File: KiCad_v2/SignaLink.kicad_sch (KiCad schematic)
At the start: 15 parts, among them SW1 SW_Wake, U2 ESP32-C3_SUPERMINI_TH, U3 DM-OLED096-636

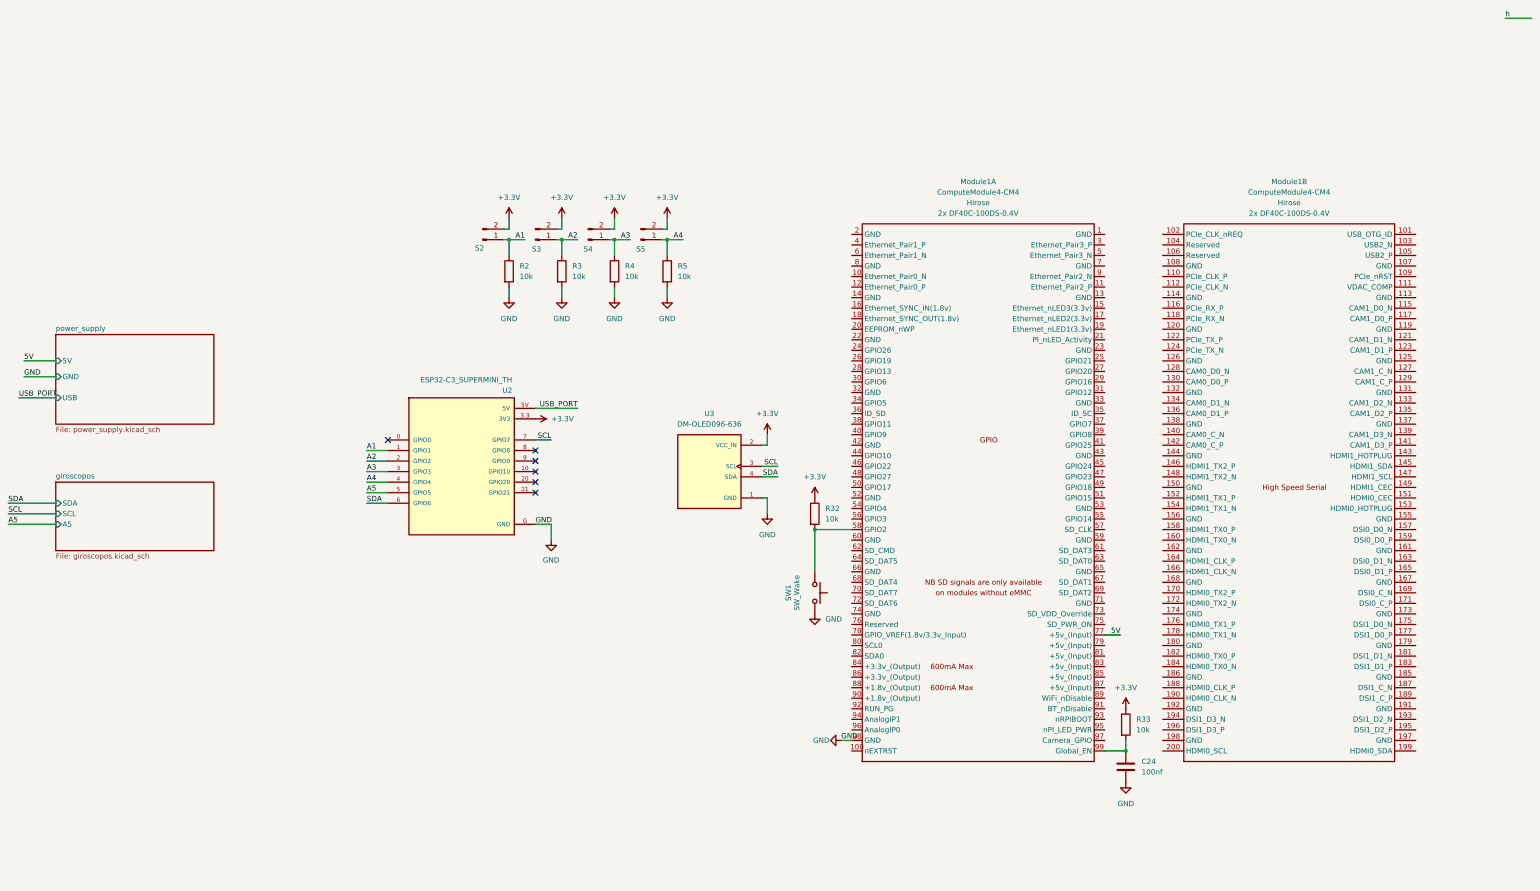
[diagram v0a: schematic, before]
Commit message: feat: huella cm4 y mcp symbols
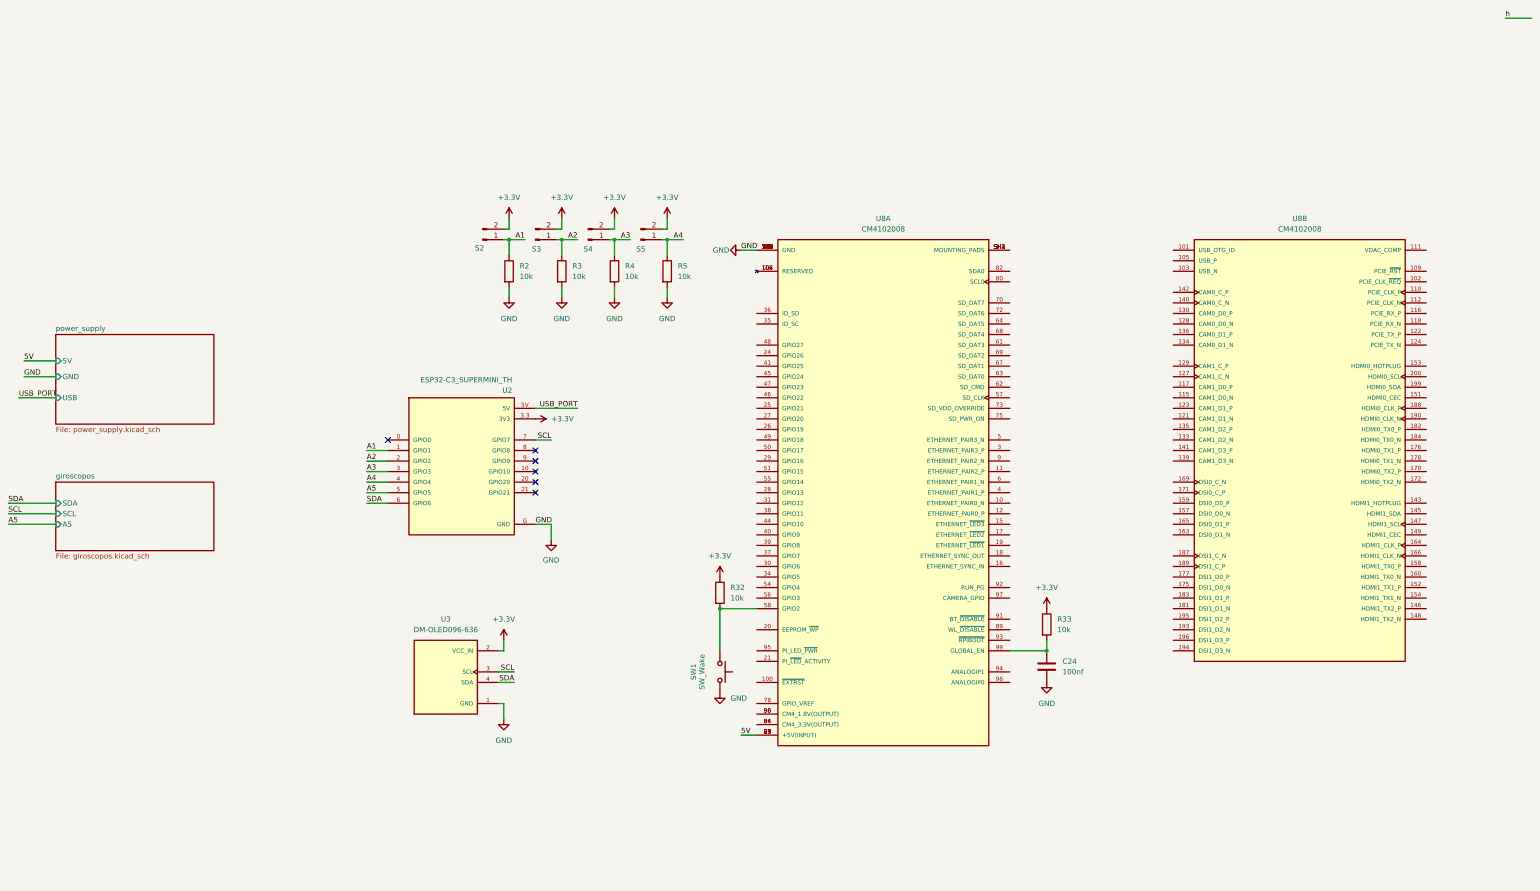
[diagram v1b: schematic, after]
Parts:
- removed Module1: ComputeModule4-CM4, CM4IO:Raspberry-Pi-4-Compute-Module, symbol CM4IO:ComputeModule4-CM4
- added U8: CM4102008, Custom_Footprints:MODULE_CM4102008, symbol CM4102008:CM4102008
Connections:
- net 5V: now also U8.77 (+5V(INPUT)), U8.79 (+5V(INPUT)), U8.81 (+5V(INPUT)), U8.83 (+5V(INPUT)), U8.85 (+5V(INPUT)), U8.87 (+5V(INPUT))
- net GND: now also U8.1 (GND), U8.107 (GND), U8.108 (GND), U8.113 (GND), U8.114 (GND), U8.119 (GND), U8.120 (GND), U8.125 (GND), U8.126 (GND), U8.13 (GND), U8.131 (GND), U8.132 (GND), U8.137 (GND), U8.138 (GND), U8.14 (GND), U8.144 (GND), U8.150 (GND), U8.155 (GND), U8.156 (GND), U8.161 (GND), U8.162 (GND), U8.167 (GND), U8.168 (GND), U8.173 (GND), U8.174 (GND), U8.179 (GND), U8.180 (GND), U8.185 (GND), U8.186 (GND), U8.191 (GND), U8.192 (GND), U8.197 (GND), U8.198 (GND), U8.2 (GND), U8.22 (GND), U8.23 (GND), U8.32 (GND), U8.33 (GND), U8.42 (GND), U8.43 (GND), U8.52 (GND), U8.53 (GND), U8.59 (GND), U8.60 (GND), U8.65 (GND), U8.66 (GND), U8.7 (GND), U8.71 (GND), U8.74 (GND), U8.8 (GND), U8.98 (GND)
- net at C24.1, R33.2: now also U8.99 (GLOBAL_EN)
- net at R32.2, SW1.1: now also U8.58 (GPIO2)
- new net: U8.104 (RESERVED), U8.106 (RESERVED), U8.76 (RESERVED)
- new net: U8.84 (CM4_3.3V(OUTPUT)), U8.86 (CM4_3.3V(OUTPUT))
- new net: U8.88 (CM4_1.8V(OUTPUT)), U8.90 (CM4_1.8V(OUTPUT))
- new net: U8.SH1 (MOUNTING_PADS), U8.SH2 (MOUNTING_PADS), U8.SH3 (MOUNTING_PADS), U8.SH4 (MOUNTING_PADS)
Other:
- moved on the sheet: C24, R32, R33, SW1, U3

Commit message: feat: comienzo rooteo y perfeccionar esquematico
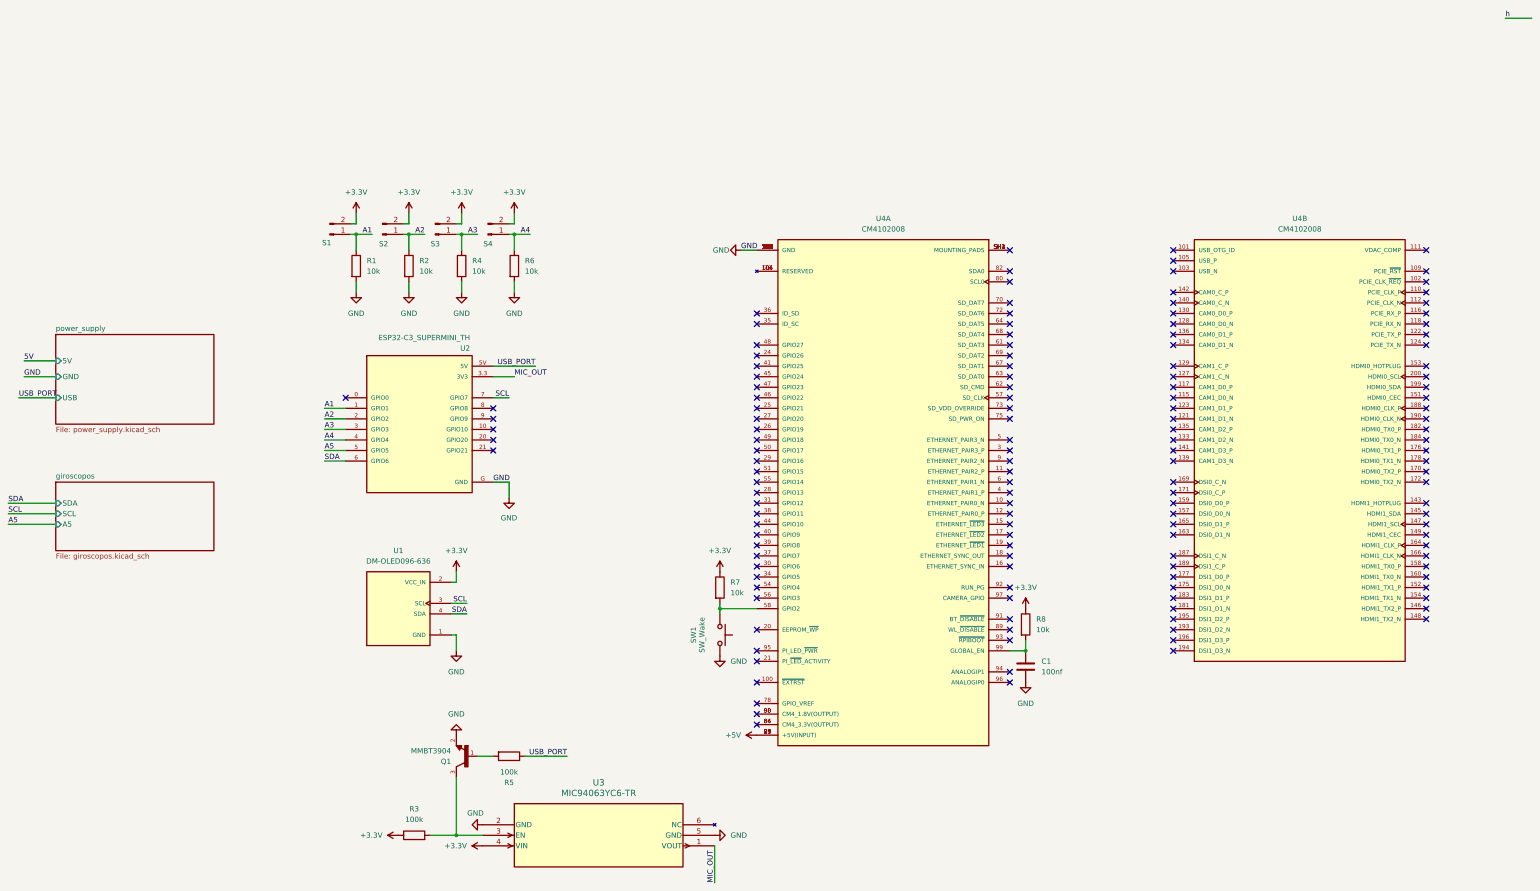
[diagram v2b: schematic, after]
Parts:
- added Q1: MMBT3904, Custom_Footprints:MMBT3904, symbol MMBT3904:MMBT3904
- added R3, R5: 100k, Resistor_SMD:R_0603_1608Metric, symbol Device:R
- added U3: MIC94063YC6-TR, Custom_Footprints:SC-70_C6_MCH-L, symbol MIC94063:MIC94063YC6-TR
- renumbered C24 to C1, R2 to R1, R3 to R2, R5 to R6, R32 to R7, R33 to R8, S2 to S1, S3 to S2, S4 to S3, S5 to S4, U3 to U1, U8 to U4
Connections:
- net +3.3V: now also R3.1, U3.4 (VIN); no longer U2.3.3 (3V3)
- net 5V: no longer U4.77 (+5V(INPUT)), U4.79 (+5V(INPUT)), U4.81 (+5V(INPUT)), U4.83 (+5V(INPUT)), U4.85 (+5V(INPUT)), U4.87 (+5V(INPUT))
- net GND: now also Q1.2, U3.2 (GND), U3.5 (GND)
- net USB_PORT: now also R5.1
- new net: Q1.1, R5.2
- new net: Q1.3, R3.2, U3.3 (EN)
- new net +5V: U4.77 (+5V(INPUT)), U4.79 (+5V(INPUT)), U4.81 (+5V(INPUT)), U4.83 (+5V(INPUT)), U4.85 (+5V(INPUT)), U4.87 (+5V(INPUT))
- new net MIC_OUT: U2.3.3 (3V3), U3.1 (VOUT)
- no-connect marks 6 -> 143
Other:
- moved on the sheet: C1, R1, R2, R4, R6, R7, R8, S1, S2, S3, S4, SW1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

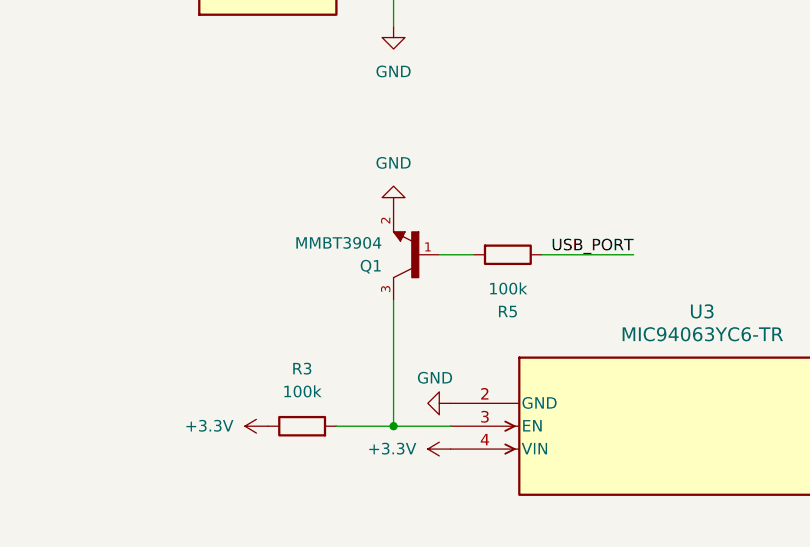
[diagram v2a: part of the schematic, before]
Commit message: feat: sigue rooteo y correccion de valores de resistencias
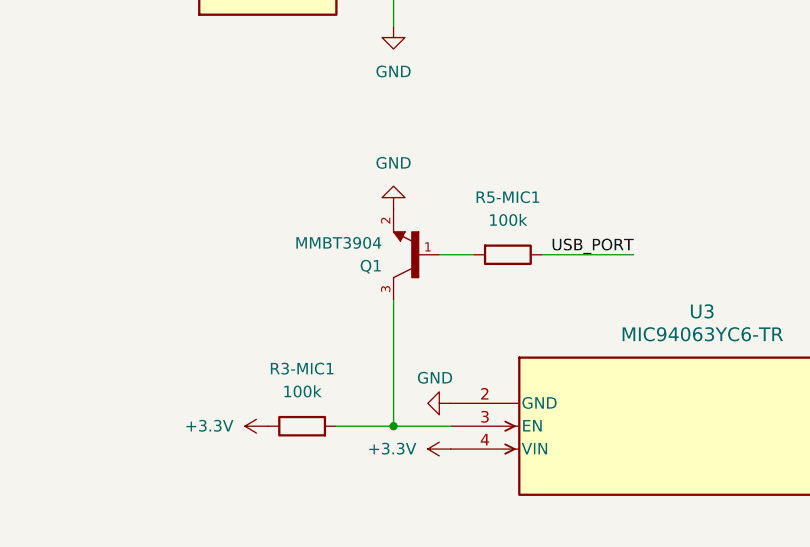
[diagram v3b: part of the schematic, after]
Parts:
- renumbered R3 to R3-MIC1, R5 to R5-MIC1
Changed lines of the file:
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@@
 		(dnp no)
 		(fields_autoplaced yes)
-		(property "Reference" "R5"
-			(at 59.69 158.75 90)
+		(property "Reference" "R5-MIC1"
+			(at 59.69 146.05 90)
 			(effects
 				(font
@@
 		)
 		(property "Value" "100k"
-			(at 59.69 156.21 90)
+			(at 59.69 148.59 90)
 			(effects
 				(font
@@
 			(project ""
 				(path "/a1f5fcc2-f8ff-418d-9afd-dd6d7b5c6dc3"
-					(reference "R5")
+					(reference "R5-MIC1")
 					(unit 1)
 				)
@@
 		(dnp no)
 		(fields_autoplaced yes)
-		(property "Reference" "R3"
+		(property "Reference" "R3-MIC1"
 			(at 36.83 165.1 90)
 			(effects
@@
 			(project ""
 				(path "/a1f5fcc2-f8ff-418d-9afd-dd6d7b5c6dc3"
-					(reference "R3")
+					(reference "R3-MIC1")
 					(unit 1)
 				)

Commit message: Placa casi finalizada
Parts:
- U2: footprint Custom_Footprints:MODULE_ESP32-C3_SUPERMINI_TH -> Custom_Footprints:MODULE_ESP32-C3_SUPERMINI
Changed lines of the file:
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@@
 			)
 		)
-		(property "Footprint" "Custom_Footprints:MODULE_ESP32-C3_SUPERMINI_TH"
+		(property "Footprint" "Custom_Footprints:MODULE_ESP32-C3_SUPERMINI"
 			(at 26.416 104.394 0)
 			(effects
